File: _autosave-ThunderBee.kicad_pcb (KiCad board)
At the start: 2 copper layers, 34.3 x 8.4 mm, 1 part, among them J1 Bus_PCI_Express_x4

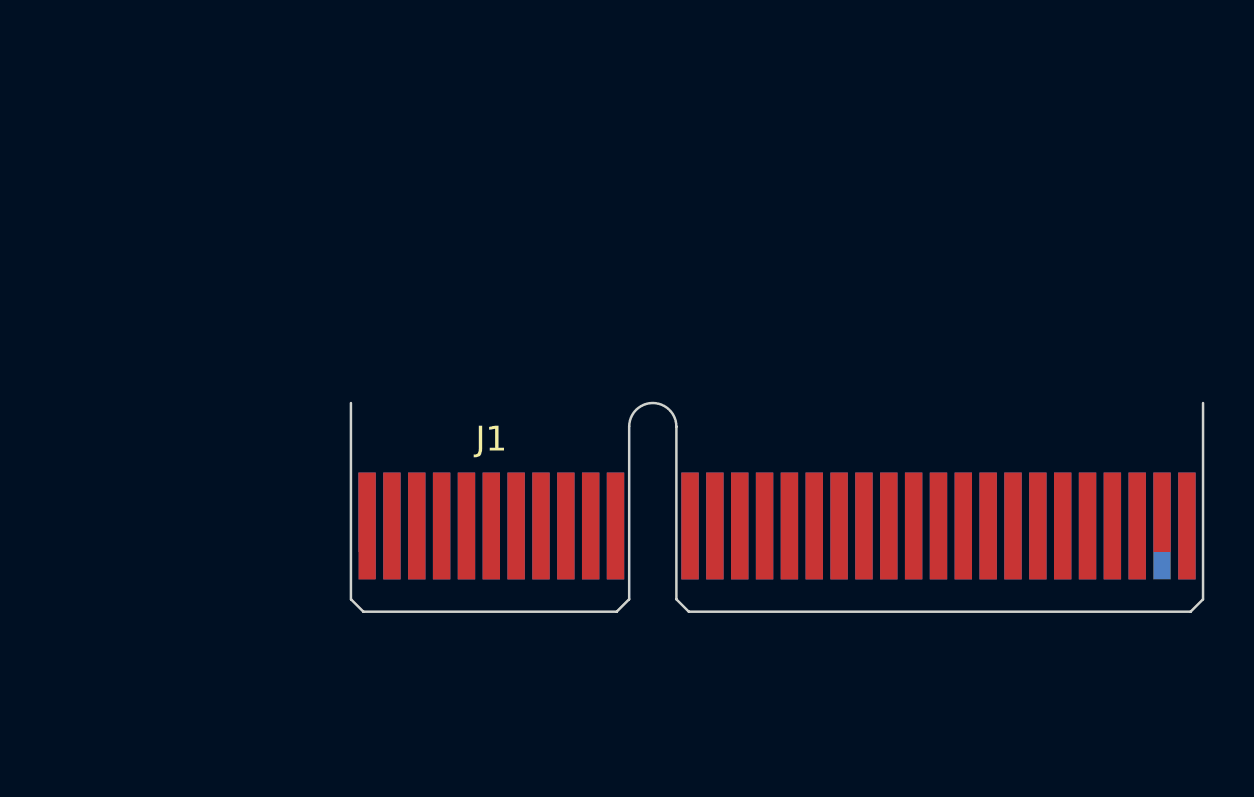
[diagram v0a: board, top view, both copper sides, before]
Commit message: DDR Labels
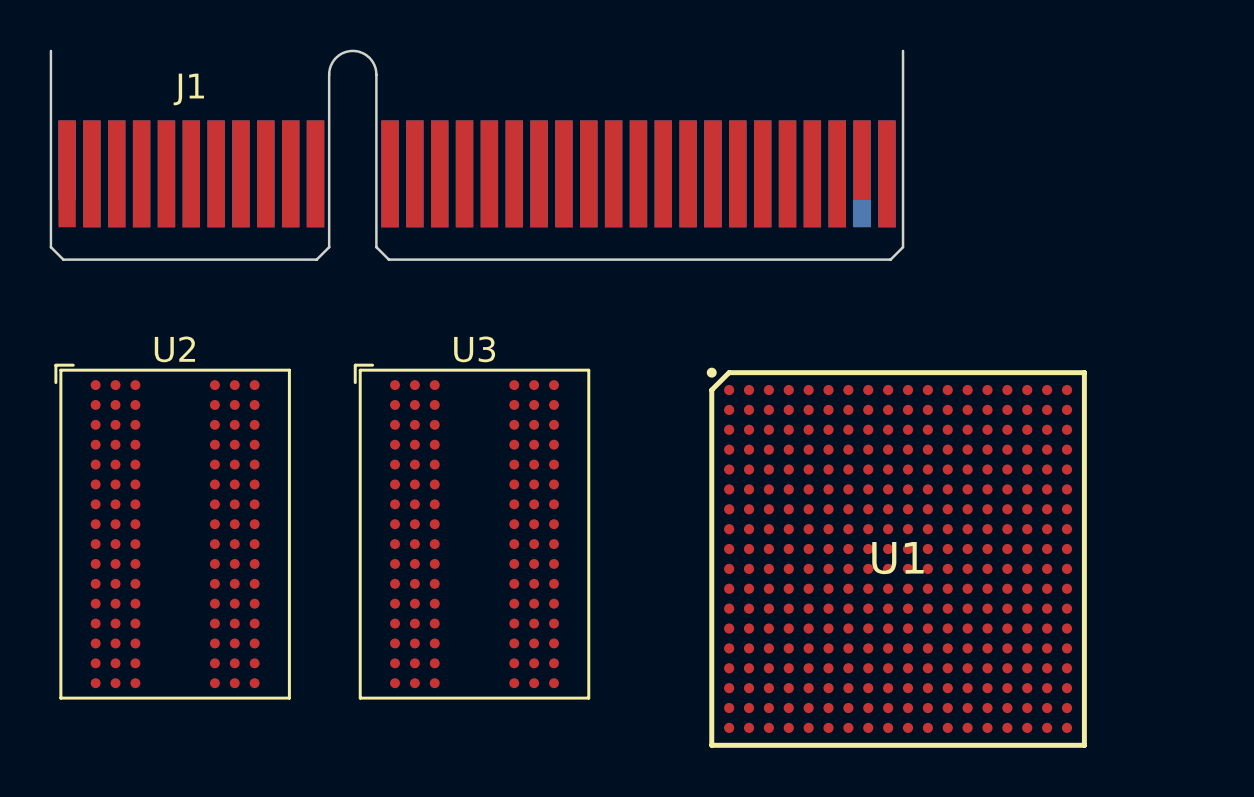
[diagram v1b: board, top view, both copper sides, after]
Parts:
- added U1: XC7A35T-CSG325, Footprints:BGA324C80P18X18_1500X1500X150, F.Cu at (119.9, 98.4)
- added U2: MT41K64M16JT-15E, Package_BGA:BGA-96_9.0x13.0mm_Layout2x3x16_P0.8mm, F.Cu at (90.8, 97.4)
- added U3: MT41K64M16JT-15E, Package_BGA:BGA-96_9.0x13.0mm_Layout2x3x16_P0.8mm, F.Cu at (102.9, 97.4)
- moved J1 18.6 mm to (86.5, 82.9)
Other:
- outline, holes or cut-outs redrawn
- copper layers 2 -> 4
